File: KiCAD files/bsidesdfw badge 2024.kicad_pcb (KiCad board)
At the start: 2 copper layers, 117.4 x 117.4 mm, 4 parts

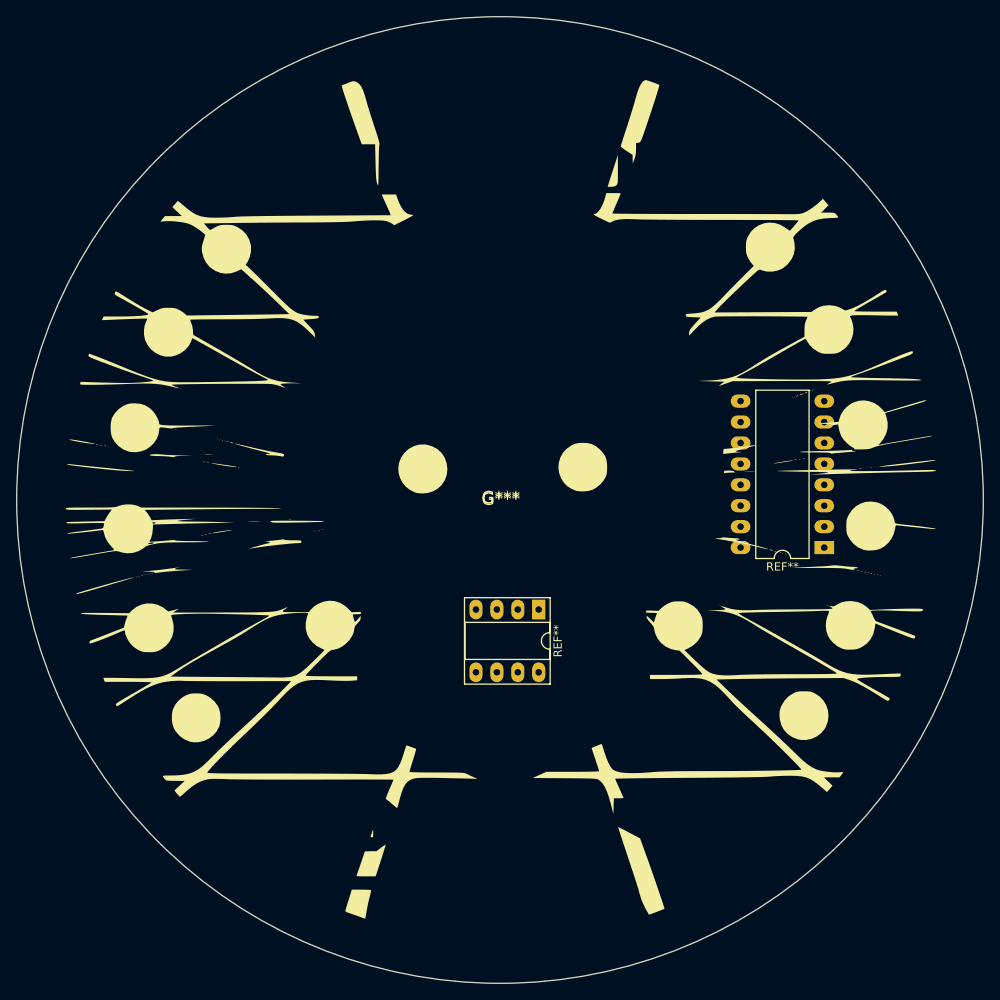
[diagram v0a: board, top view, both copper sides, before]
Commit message: add some various board footprints to PCB for initial layouts
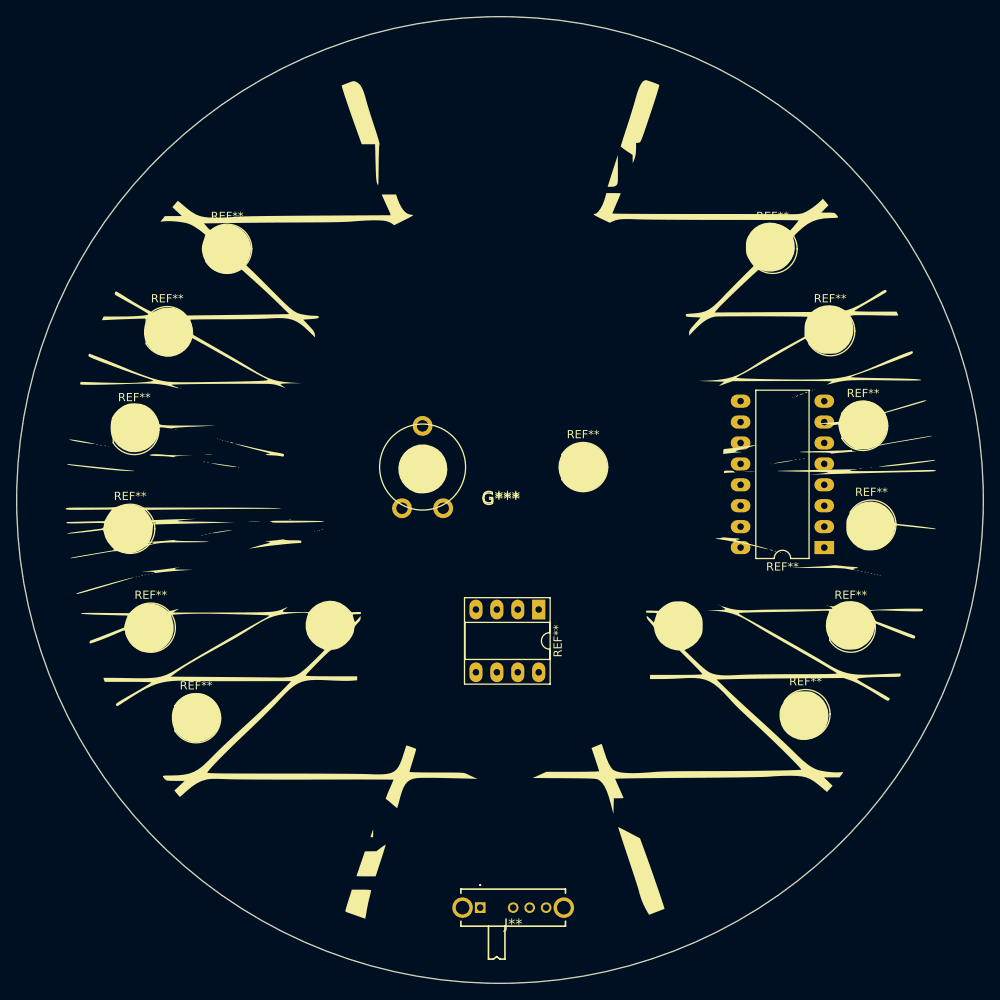
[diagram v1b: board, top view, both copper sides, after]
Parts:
- added J**: SLW12745474ARAD, SamacSys_Parts:SLW12745474ARAD, F.Cu at (135.0, 146.0)
- added REF**: LED_D5.0mm, LED_THT:LED_D5.0mm, F.Cu at (178.7, 112.0)
- added REF**: LED_D5.0mm, LED_THT:LED_D5.0mm, F.Cu at (99.2, 123.0)
- added REF**: LED_D5.0mm, LED_THT:LED_D5.0mm, F.Cu at (169.2, 66.0)
- added REF**: LED_D5.0mm, LED_THT:LED_D5.0mm, F.Cu at (181.2, 99.5)
- added REF**: LED_D5.0mm, LED_THT:LED_D5.0mm, F.Cu at (146.2, 92.5)
- added REF**: PT10RV10-103A0505-PM-S trim resistor, SamacSys_Parts:PT10RV10-103A0505-PM-S trim resistor, F.Cu at (128.0, 92.5)
- added REF**: LED_D5.0mm, LED_THT:LED_D5.0mm, F.Cu at (176.2, 76.0)
- added REF**: LED_D5.0mm, LED_THT:LED_D5.0mm, F.Cu at (180.2, 87.5)
- added REF**: LED_D5.0mm, LED_THT:LED_D5.0mm, F.Cu at (173.2, 122.5)
- added REF**: LED_D5.0mm, LED_THT:LED_D5.0mm, F.Cu at (93.7, 112.0)
- added REF**: LED_D5.0mm, LED_THT:LED_D5.0mm, F.Cu at (91.7, 88.0)
- added REF**: LED_D5.0mm, LED_THT:LED_D5.0mm, F.Cu at (103.0, 66.0)
- added REF**: LED_D5.0mm, LED_THT:LED_D5.0mm, F.Cu at (91.2, 100.0)
- added REF**: LED_D5.0mm, LED_THT:LED_D5.0mm, F.Cu at (95.7, 76.0)

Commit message: corrected the pin numbering for the trim resistor footprint; updated schematic to reflect trim properly
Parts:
- removed the REF** at (128.0, 92.5)
- added R2: 10k, SamacSys_Parts:PT10RV10-103A0505-PM-S trim resistor, F.Cu at (128.0, 92.5)
- renumbered J** to SW1, REF** to U1, REF** to U2
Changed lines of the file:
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@@
 		(descr "8-lead though-hole mounted DIP package, row spacing 7.62 mm (300 mils), Socket, LongPads")
 		(tags "THT DIP DIL PDIP 2.54mm 7.62mm 300mil Socket LongPads")
-		(property "Reference" "REF**"
+		(property "Reference" "U1"
 			(at 3.81 -2.33 90)
 			(layer "F.SilkS")
@@
 		(descr "16-lead though-hole mounted DIP package, row spacing 10.16 mm (400 mils), LongPads")
 		(tags "THT DIP DIL PDIP 2.54mm 10.16mm 400mil LongPads")
-		(property "Reference" "REF**"
+		(property "Reference" "U2"
 			(at 5.08 -2.33 0)
 			(layer "F.SilkS")
@@
 		)
 	)
+	(footprint "SamacSys_Parts:PT10RV10-103A0505-PM-S trim resistor"
+		(layer "F.Cu")
+		(at 128 92.5)
+		(property "Reference" "R2"
+			(at 0 -0.5 0)
+			(unlocked yes)
+			(layer "F.SilkS")
+			(effects
+				(font
+					(size 1 1)
+					(thickness 0.1)
+				)
+			)
+		)
+		(property "Value" "10k"
+			(at 0 1 0)
+			(unlocked yes)
+			(layer "F.Fab")
+			(effects
+				(font
+					(size 1 1)
+					(thickness 0.15)
+				)
+			)
+		)
+		(property "Footprint" ""
+			(at 0 0 0)
+			(unlocked yes)
+			(layer "F.Fab")
+			(hide yes)
+			(effects
+				(font
+					(size 1 1)
+					(thickness 0.15)
+				)
+			)
+		)
+		(property "Datasheet" ""
+			(at 0 0 0)
+			(unlocked yes)
+			(layer "F.Fab")
+			(hide yes)
+			(effects
+				(font
+					(size 1 1)
+					(thickness 0.15)
+				)
+			)
+		)
+		(property "Description" ""
+			(at 0 0 0)
+			(unlocked yes)
+			(layer "F.Fab")
+			(hide yes)
+			(effects
+				(font
+					(size 1 1)
+					(thickness 0.15)
+				)
+			)
+		)
+		(attr through_hole)
+		(fp_circle
+			(center 0 0)
+			(end 1.5 1.5)
+			(stroke
+				(width 0.1)
+				(type default)
+			)
+			(fill none)
+			(layer "F.SilkS")
+		)
+		(fp_circle
+			(center 0 0)
+			(end 5 1.5)
+			(stroke
+				(width 0.1)
+				(type default)
+			)
+			(fill none)
+			(layer "F.SilkS")
+		)
+		(fp_text user "${REFERENCE}"
+			(at 0 2.5 0)
+			(unlocked yes)
+			(layer "F.Fab")
+			(effects
+				(font
+					(size 1 1)
+					(thickness 0.15)
+				)
+			)
+		)
+		(pad "1" thru_hole circle
+			(at -2.5 5)
+			(size 2.4 2.4)
+			(drill 1.4)
+			(layers "*.Cu" "*.Mask")
+			(remove_unused_layers no)
+		)
+		(pad "2" thru_hole circle
+			(at 0 -5)
+			(size 2.4 2.4)
+			(drill 1.4)
+			(layers "*.Cu" "*.Mask")
+			(remove_unused_layers no)
+		)
+		(pad "3" thru_hole circle
+			(at 2.5 5)
+			(size 2.4 2.4)
+			(drill 1.4)
+			(layers "*.Cu" "*.Mask")
+			(remove_unused_layers no)
+		)
+	)
 	(footprint "LED_THT:LED_D5.0mm"
 		(layer "F.Cu")
@@
 		)
 	)
-	(footprint "SamacSys_Parts:PT10RV10-103A0505-PM-S trim resistor"
-		(layer "F.Cu")
-		(at 128 92.5)
-		(property "Reference" "REF**"
-			(at 0 -0.5 0)
-			(unlocked yes)
-			(layer "F.SilkS")
-			(effects
-				(font
-					(size 1 1)
-					(thickness 0.1)
-				)
-			)
-		)
-		(property "Value" "PT10RV10-103A0505-PM-S trim resistor"
-			(at 0 1 0)
-			(unlocked yes)
-			(layer "F.Fab")
-			(effects
-				(font
-					(size 1 1)
-					(thickness 0.15)
-				)
-			)
-		)
-		(property "Footprint" ""
-			(at 0 0 0)
-			(unlocked yes)
-			(layer "F.Fab")
-			(hide yes)
-			(effects
-				(font
-					(size 1 1)
-					(thickness 0.15)
-				)
-			)
-		)
-		(property "Datasheet" ""
-			(at 0 0 0)
-			(unlocked yes)
-			(layer "F.Fab")
-			(hide yes)
-			(effects
-				(font
-					(size 1 1)
-					(thickness 0.15)
-				)
-			)
-		)
-		(property "Description" ""
-			(at 0 0 0)
-			(unlocked yes)
-			(layer "F.Fab")
-			(hide yes)
-			(effects
-				(font
-					(size 1 1)
-					(thickness 0.15)
-				)
-			)
-		)
-		(attr through_hole)
-		(fp_circle
-			(center 0 0)
-			(end 1.5 1.5)
-			(stroke
-				(width 0.1)
-				(type default)
-			)
-			(fill none)
-			(layer "F.SilkS")
-		)
-		(fp_circle
-			(center 0 0)
-			(end 5 1.5)
-			(stroke
-				(width 0.1)
-				(type default)
-			)
-			(fill none)
-			(layer "F.SilkS")
-		)
-		(fp_text user "${REFERENCE}"
-			(at 0 2.5 0)
-			(unlocked yes)
-			(layer "F.Fab")
-			(effects
-				(font
-					(size 1 1)
-					(thickness 0.15)
-				)
-			)
-		)
-		(pad "1" thru_hole circle
-			(at 0 -5)
-			(size 2.4 2.4)
-			(drill 1.4)
-			(layers "*.Cu" "*.Mask")
-			(remove_unused_layers no)
-		)
-		(pad "2" thru_hole circle
-			(at -2.5 5)
-			(size 2.4 2.4)
-			(drill 1.4)
-			(layers "*.Cu" "*.Mask")
-			(remove_unused_layers no)
-		)
-		(pad "3" thru_hole circle
-			(at 2.5 5)
-			(size 2.4 2.4)
-			(drill 1.4)
-			(layers "*.Cu" "*.Mask")
-			(remove_unused_layers no)
-		)
-	)
 	(footprint "LED_THT:LED_D5.0mm"
 		(layer "F.Cu")
@@
 		(descr "SLW-1274547-4A-RA-D-2")
 		(tags "Connector")
-		(property "Reference" "J**"
-			(at 4 2 360)
+		(property "Reference" "SW1"
+			(at 4 2 0)
 			(layer "F.SilkS")
 			(effects
@@
 		)
 		(property "Value" "SLW12745474ARAD"
-			(at 4 2 360)
+			(at 4 2 0)
 			(layer "F.SilkS")
 			(hide yes)
@@
 		)
 		(property "Footprint" ""
-			(at 0 0 360)
+			(at 0 0 0)
 			(layer "F.Fab")
 			(hide yes)
@@
 		)
 		(property "Datasheet" ""
-			(at 0 0 360)
+			(at 0 0 0)
 			(layer "F.Fab")
 			(hide yes)
@@
 		)
 		(property "Description" ""
-			(at 0 0 360)
+			(at 0 0 0)
 			(layer "F.Fab")
 			(hide yes)
@@
 		)
 		(fp_text user "${REFERENCE}"
-			(at 4 2 360)
+			(at 4 2 0)
 			(layer "F.Fab")
 			(effects

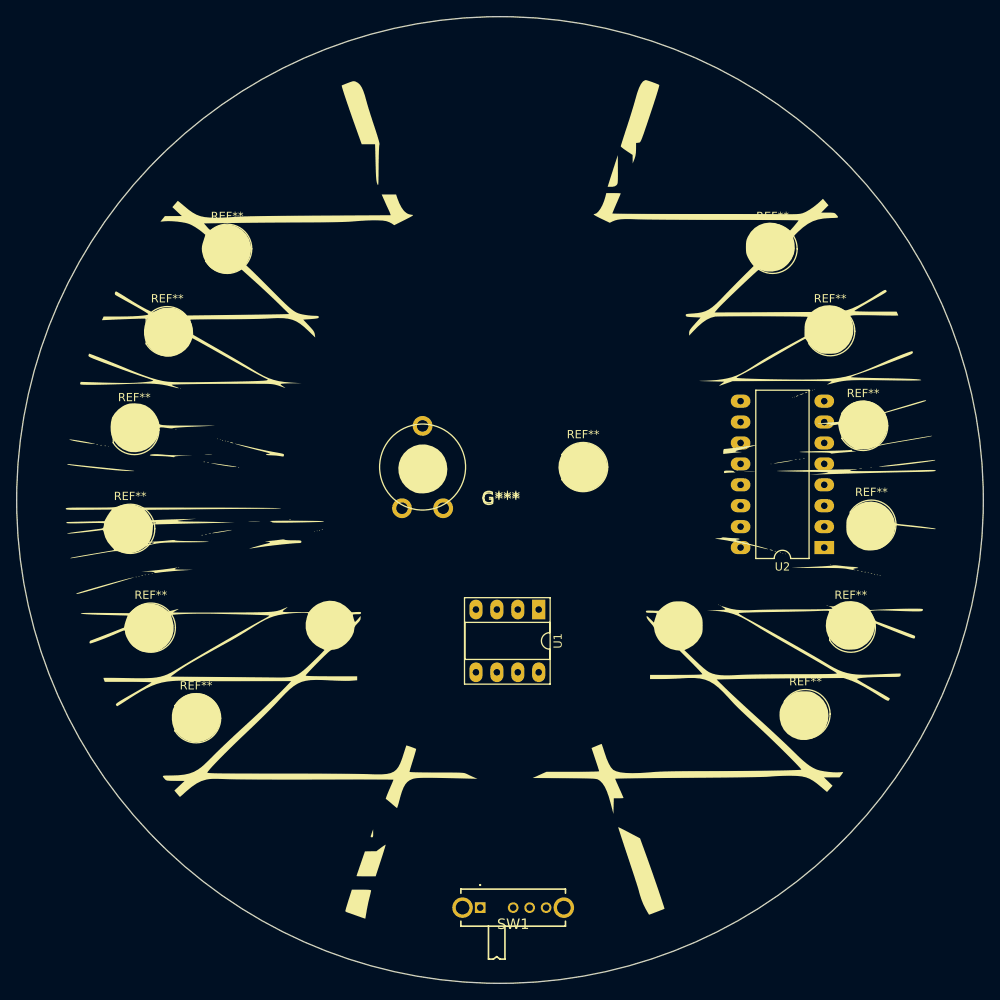
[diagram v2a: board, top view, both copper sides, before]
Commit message: fixed broken footprint assignments; laid out components. Added a diode for reverse polarity protection.
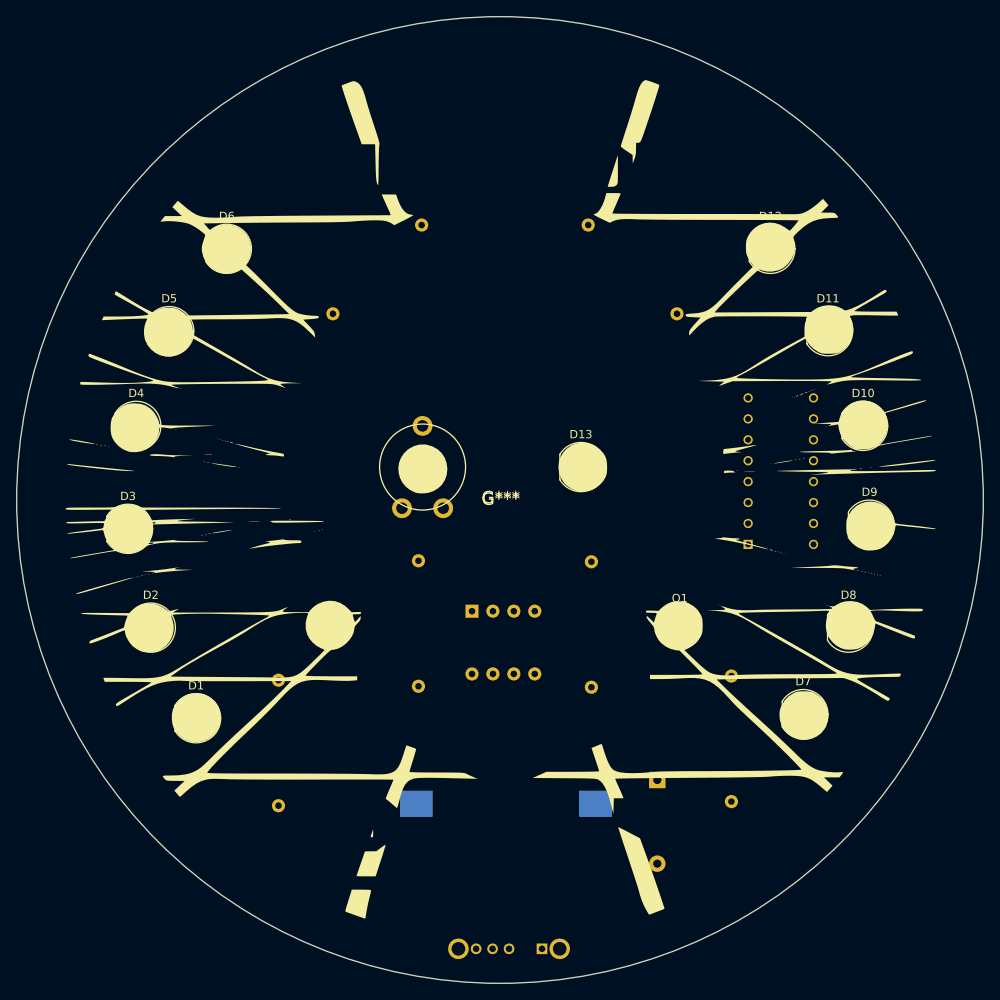
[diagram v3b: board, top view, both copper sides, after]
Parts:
- removed REF** (x13): LED_D5.0mm, LED_THT:LED_D5.0mm
- added BT1: 6v, SamacSys_Parts:1062, B.Cu at (138.1, 133.4)
- added C1: 4.7uF, Capacitor_THT:CP_Radial_D4.0mm_P1.50mm, B.Cu at (117.5, 111.5)
- added D1: ~, LED_THT:LED_D5.0mm, F.Cu at (99.2, 123.0)
- added D10: ~, LED_THT:LED_D5.0mm, F.Cu at (180.2, 87.5)
- added D11: ~, LED_THT:LED_D5.0mm, F.Cu at (176.0, 76.0)
- added D12: ~, LED_THT:LED_D5.0mm, F.Cu at (169.0, 66.0)
- added D13: ~, LED_THT:LED_D5.0mm, F.Cu at (146.0, 92.5)
- added D14: D, Diode_THT:D_T-1_P10.16mm_Horizontal, B.Cu at (156.5, 130.5)
- added D2: ~, LED_THT:LED_D5.0mm, F.Cu at (93.7, 112.0)
- added D3: ~, LED_THT:LED_D5.0mm, F.Cu at (91.0, 100.0)
- added D4: ~, LED_THT:LED_D5.0mm, F.Cu at (92.0, 87.5)
- added D5: ~, LED_THT:LED_D5.0mm, F.Cu at (96.0, 76.0)
- added D6: ~, LED_THT:LED_D5.0mm, F.Cu at (103.0, 66.0)
- added D7: ~, LED_THT:LED_D5.0mm, F.Cu at (173.0, 122.5)
- added D8: ~, LED_THT:LED_D5.0mm, F.Cu at (178.5, 112.0)
- added D9: ~, LED_THT:LED_D5.0mm, F.Cu at (181.0, 99.5)
- added Q1: BC548, Package_TO_SOT_THT:TO-92_Inline, F.Cu at (158.0, 112.0)
- added R1: 10k, Resistor_THT:R_Axial_DIN0309_L9.0mm_D3.2mm_P15.24mm_Horizontal, B.Cu at (127.5, 119.1)
- added R3: 10k, Resistor_THT:R_Axial_DIN0309_L9.0mm_D3.2mm_P15.24mm_Horizontal, B.Cu at (148.1, 63.1)
- added R4: 10k, Resistor_THT:R_Axial_DIN0309_L9.0mm_D3.2mm_P15.24mm_Horizontal, B.Cu at (148.5, 104.0)
- added R5: 1M, Resistor_THT:R_Axial_DIN0309_L9.0mm_D3.2mm_P15.24mm_Horizontal, B.Cu at (165.5, 133.1)
- added R6: 68 Ohm, Resistor_THT:R_Axial_DIN0309_L9.0mm_D3.2mm_P15.24mm_Horizontal, B.Cu at (110.5, 133.6)
- added R7: 68 Ohm, Resistor_THT:R_Axial_DIN0309_L9.0mm_D3.2mm_P15.24mm_Horizontal, B.Cu at (117.1, 73.9)
- R2: value 10k -> trim
- SW1: value SLW12745474ARAD -> SW_SPDT_312; moved to B.Cu
- U1: value DIP-8_W7.62mm_Socket_LongPads -> NE555P; footprint Package_DIP:DIP-8_W7.62mm_Socket_LongPads -> Package_DIP:DIP-8_W7.62mm; moved to B.Cu
- U2: value DIP-16_W10.16mm_LongPads -> 74HC595; footprint Package_DIP:DIP-16_W10.16mm_LongPads -> SamacSys_Parts:DIP794W53P254L1930H508Q16N; moved to B.Cu
- moved U2 10.7 mm to (171.5, 93.0), turned to 0 degrees
- moved SW1 9.01 mm to (142.5, 151.0), turned to 180 degrees
- moved U1 8.10 mm to (134.0, 110.0)
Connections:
- R2 pad 1: (no net) -> Net-(U1-DIS)
- R2 pad 2: (no net) -> Net-(U1-THR)
- R2 pad 3: (no net) -> unconnected-(R2-Pad3)
- SW1 pad 1: (no net) -> Net-(BT1-+)
- SW1 pad 2: (no net) -> Net-(D14-A)
- SW1 pad 3: (no net) -> unconnected-(SW1-A-Pad3)
- U1 pad 1: (no net) -> GND
- U1 pad 2: (no net) -> Net-(U1-THR)
- U1 pad 3: (no net) -> Net-(U1-Q)
- U1 pad 4: (no net) -> +6V
- U1 pad 5: (no net) -> unconnected-(U1-CV-Pad5)
- U1 pad 6: (no net) -> Net-(U1-THR)
- U1 pad 7: (no net) -> Net-(U1-DIS)
- U1 pad 8: (no net) -> +6V
- U2 pad 1: (no net) -> Net-(D2-K)
- U2 pad 10: (no net) -> +6V
- U2 pad 11: (no net) -> Net-(U1-Q)
- U2 pad 12: (no net) -> Net-(U2-RCLK)
- U2 pad 13: (no net) -> GND
- U2 pad 14: (no net) -> Net-(Q1-C)
- U2 pad 15: (no net) -> Net-(D1-K)
- U2 pad 16: (no net) -> +6V
- U2 pad 2: (no net) -> Net-(D3-K)
- U2 pad 3: (no net) -> Net-(D4-K)
- U2 pad 4: (no net) -> Net-(D10-K)
- U2 pad 5: (no net) -> Net-(D11-K)
- U2 pad 6: (no net) -> Net-(D12-K)
- U2 pad 7: (no net) -> unconnected-(U2-QH-Pad7)
- U2 pad 8: (no net) -> GND
- U2 pad 9: (no net) -> Net-(U2-QH')

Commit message: placement finalized; tentative lanyard hole
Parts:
- Q1: moved to B.Cu
- moved R7 15.8 mm to (128.5, 63.0), turned to -135 degrees
- moved Q1 2.54 mm to (160.5, 112.0), turned to 180 degrees
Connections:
- SW1 pad 1: Net-(BT1-+) -> Net-(D14-A)
- SW1 pad 2: Net-(D14-A) -> Net-(BT1-+)
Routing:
- net (no net): track 0.00 -> 34.7 mm
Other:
- outline, holes or cut-outs redrawn
